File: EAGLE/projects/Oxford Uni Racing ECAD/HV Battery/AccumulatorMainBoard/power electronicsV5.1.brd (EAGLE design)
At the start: 167.6 x 103.8 mm, 82 parts, among them IC1 4043D, IC2 SE555D, IC9 4011D, K2 T9AS5D12-12=T9A, K6 T9AS1D12-48=T9A, K7 T9AS1D12-48=T9A, Q1 BSS138, Q2 BSS138, Q3 BSS138, Q4 BSS138

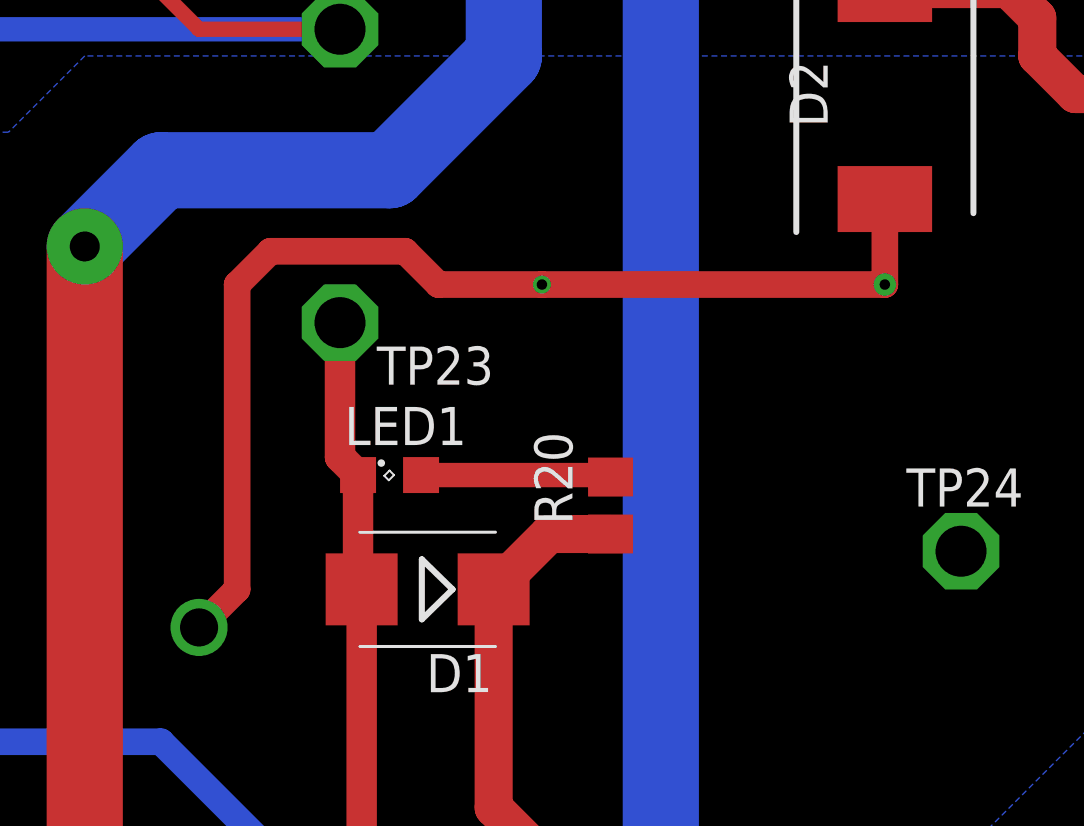
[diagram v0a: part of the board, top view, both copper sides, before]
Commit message: Mainboard v5.1
Fixes the +12V  connections
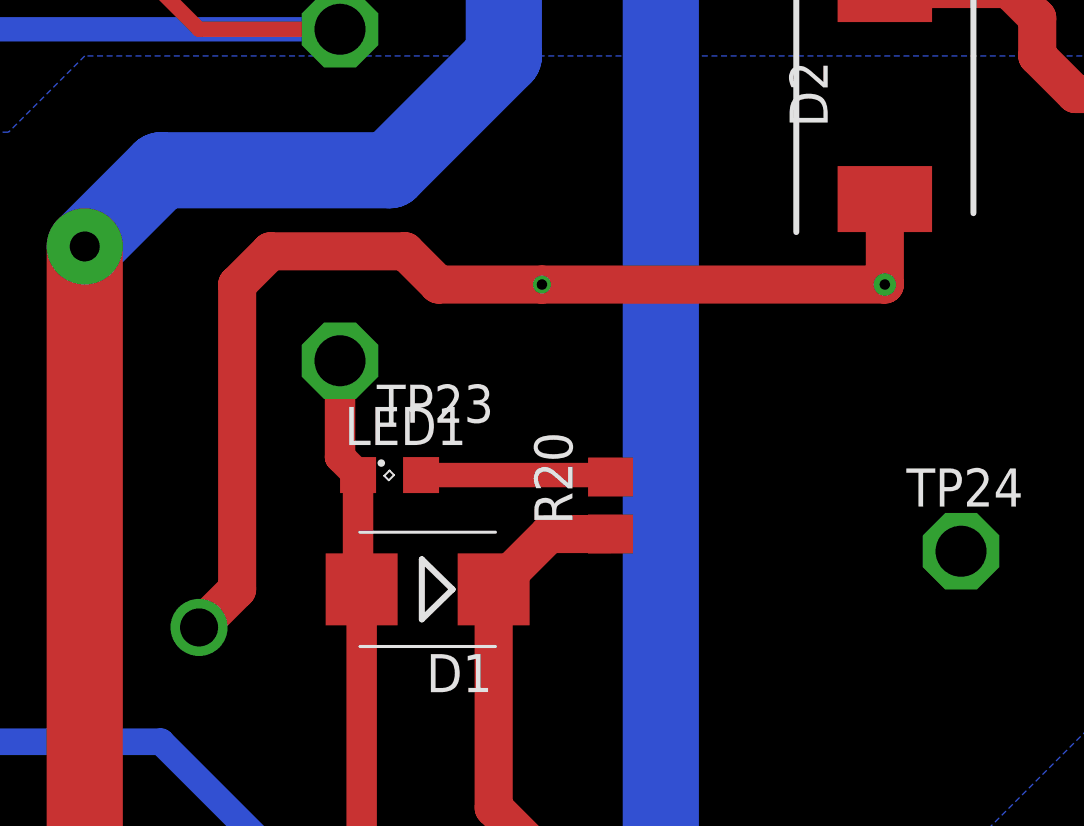
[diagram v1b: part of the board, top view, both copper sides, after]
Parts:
- moved TP23 1.27 mm to (93.6, 54.6)
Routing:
- net PRECHARGE_SELECT: track 133.7 -> 132.4 mm
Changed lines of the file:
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@@
 <attribute name="VALUE" x="40.132" y="52.832" size="0.0254" layer="27"/>
 </element>
-<element name="TP23" library="testpad" library_urn="urn:adsk.eagle:library:385" package="P1-17" package3d_urn="urn:adsk.eagle:package:27949/1" value="TPPAD1-17" x="93.599" y="55.88" smashed="yes">
-<attribute name="NAME" x="94.8271" y="53.8129" size="1.27" layer="25"/>
-<attribute name="POPULARITY" value="0" x="93.599" y="55.88" size="1.778" layer="27" display="off"/>
-<attribute name="TP_SIGNAL_NAME" value="" x="93.599" y="53.975" size="1" layer="37"/>
-<attribute name="VALUE" x="89.281" y="55.372" size="0.0254" layer="27"/>
+<element name="TP23" library="testpad" library_urn="urn:adsk.eagle:library:385" package="P1-17" package3d_urn="urn:adsk.eagle:package:27949/1" value="TPPAD1-17" x="93.599" y="54.61" smashed="yes">
+<attribute name="NAME" x="94.8271" y="52.5429" size="1.27" layer="25"/>
+<attribute name="POPULARITY" value="0" x="93.599" y="54.61" size="1.778" layer="27" display="off"/>
+<attribute name="TP_SIGNAL_NAME" value="" x="93.599" y="52.705" size="1" layer="37"/>
+<attribute name="VALUE" x="89.281" y="54.102" size="0.0254" layer="27"/>
 </element>
 <element name="TP4" library="testpad" library_urn="urn:adsk.eagle:library:385" package="P1-17" package3d_urn="urn:adsk.eagle:package:27949/1" value="TPPAD1-17" x="93.599" y="65.659" smashed="yes">
@@
 <wire x1="76.515" y1="68.834" x2="76.581" y2="68.834" width="1.016" layer="1"/>
 <via x="76.581" y="68.834" extent="1-16" drill="0.65" diameter="1.3"/>
-<wire x1="111.76" y1="60" x2="111.76" y2="57.15" width="0.889" layer="1"/>
+<wire x1="111.76" y1="60" x2="111.76" y2="57.15" width="1.27" layer="1"/>
 <via x="111.76" y="57.15" extent="1-16" drill="0.35" diameter="0.75"/>
 <wire x1="124.841" y1="60" x2="123.19" y2="58.349" width="0.889" layer="1"/>
@@
 <wire x1="80.01" y1="67.31" x2="80.01" y2="62.23" width="0.889" layer="1"/>
 <via x="80.01" y="62.23" extent="1-16" drill="0.6"/>
-<wire x1="88.9" y1="45.72" x2="90.17" y2="46.99" width="0.889" layer="1"/>
-<wire x1="90.17" y1="46.99" x2="90.17" y2="57.15" width="0.889" layer="1"/>
-<wire x1="90.17" y1="57.15" x2="91.27885" y2="58.25885" width="0.889" layer="1"/>
-<wire x1="91.27885" y1="58.25885" x2="95.7709375" y2="58.25885" width="0.889" layer="1"/>
-<wire x1="95.7709375" y1="58.25885" x2="96.8797875" y2="57.15" width="0.889" layer="1"/>
-<wire x1="96.8797875" y1="57.15" x2="100.33" y2="57.15" width="0.889" layer="1"/>
-<wire x1="100.33" y1="57.15" x2="111.76" y2="57.15" width="0.889" layer="1"/>
+<wire x1="88.9" y1="45.72" x2="90.17" y2="46.99" width="1.27" layer="1"/>
+<wire x1="90.17" y1="46.99" x2="90.17" y2="57.15" width="1.27" layer="1"/>
+<wire x1="90.17" y1="57.15" x2="91.27885" y2="58.25885" width="1.27" layer="1"/>
+<wire x1="91.27885" y1="58.25885" x2="95.7709375" y2="58.25885" width="1.27" layer="1"/>
+<wire x1="95.7709375" y1="58.25885" x2="96.8797875" y2="57.15" width="1.27" layer="1"/>
+<wire x1="96.8797875" y1="57.15" x2="100.33" y2="57.15" width="1.27" layer="1"/>
+<wire x1="100.33" y1="57.15" x2="111.76" y2="57.15" width="1.27" layer="1"/>
 </signal>
 <signal name="N$3" class="2">
@@
 <wire x1="94.2" y1="47.11" x2="94.2" y2="50.8" width="1.016" layer="1"/>
 <wire x1="94.2" y1="50.8" x2="93.599" y2="51.401" width="1.016" layer="1"/>
-<wire x1="93.599" y1="51.401" x2="93.599" y2="55.88" width="1.016" layer="1"/>
+<wire x1="93.599" y1="51.401" x2="93.599" y2="54.61" width="1.016" layer="1"/>
 <wire x1="8.89" y1="71.3486" x2="38.3286" y2="41.91" width="0.889" layer="16"/>
 <wire x1="38.3286" y1="41.91" x2="87.63" y2="41.91" width="0.889" layer="16"/>

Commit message: Final mainboard design
final mainboard design. v5.1
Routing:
- net +12V: track 147.5 -> 132.4 mm
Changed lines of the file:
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@@
 <attribute name="POPULARITY" value="0" x="59.309" y="47.879" size="1.778" layer="27" display="off"/>
 <attribute name="TP_SIGNAL_NAME" value="" x="59.309" y="47.879" size="1.778" layer="27" display="off"/>
-<attribute name="VALUE" x="59.309" y="46.609" size="0.0254" layer="27"/>
+<attribute name="VALUE" x="59.309" y="46.609" size="0.0254" layer="1"/>
 </element>
 <element name="TP11" library="testpad" library_urn="urn:adsk.eagle:library:385" package="P1-17" package3d_urn="urn:adsk.eagle:package:27949/1" value="TPPAD1-17" x="54.483" y="84.836" smashed="yes">
@@
 <wire x1="98.72" y1="46.99" x2="100.564" y2="48.834" width="1.27" layer="1"/>
 <wire x1="100.564" y1="48.834" x2="102.616" y2="48.834" width="1.27" layer="1"/>
-<wire x1="66.04" y1="31.75" x2="66.04" y2="44.282" width="1.27" layer="1"/>
-<wire x1="66.04" y1="44.282" x2="76.454" y2="54.696" width="1.27" layer="1"/>
 <wire x1="30.48" y1="31.75" x2="30.48" y2="45.38" width="1.27" layer="1"/>
 <wire x1="30.48" y1="45.38" x2="30.82" y2="45.72" width="1.27" layer="1"/>
@@
 <vertex x="133.35" y="60.96"/>
 <vertex x="129.54" y="64.77"/>
-<vertex x="85.09" y="64.77"/>
-<vertex x="82.55" y="62.23"/>
-<vertex x="81.28" y="62.23"/>
+<vertex x="78.74" y="64.77"/>
 <vertex x="77.47" y="66.04"/>
-<vertex x="77.47" y="71.12"/>
-<vertex x="76.2" y="72.39"/>
+<vertex x="77.47" y="72.39"/>
 <vertex x="72.39" y="72.39"/>
 <vertex x="69.85" y="69.85"/>
@@
 <wire x1="107.95" y1="30.48" x2="98.72" y2="39.71" width="1.27" layer="1"/>
 <via x="100.33" y="57.15" extent="1-16" drill="0.35"/>
-<wire x1="72.39" y1="45.72" x2="68.58" y2="41.91" width="2.54" layer="1"/>
-<wire x1="68.58" y1="34.29" x2="66.04" y2="31.75" width="2.54" layer="1"/>
-<wire x1="68.58" y1="41.91" x2="68.58" y2="34.29" width="2.54" layer="1"/>
-<via x="72.39" y="45.72" extent="1-16" drill="1.27"/>
+<wire x1="72.39" y1="38.1" x2="66.04" y2="31.75" width="2.54" layer="1"/>
+<wire x1="72.39" y1="45.72" x2="72.39" y2="38.1" width="2.54" layer="1"/>
 <via x="88.9" y="45.72" extent="1-16" drill="1.27"/>
 <wire x1="76.581" y1="68.834" x2="78.486" y2="68.834" width="0.889" layer="1"/>
@@
 <wire x1="96.8797875" y1="57.15" x2="100.33" y2="57.15" width="1.27" layer="1"/>
 <wire x1="100.33" y1="57.15" x2="111.76" y2="57.15" width="1.27" layer="1"/>
+<wire x1="72.39" y1="45.72" x2="72.39" y2="53.172" width="0.889" layer="1"/>
+<wire x1="76.454" y1="54.696" x2="73.914" y2="54.696" width="0.889" layer="1"/>
+<wire x1="73.914" y1="54.696" x2="72.39" y2="53.172" width="0.889" layer="1"/>
+<via x="72.39" y="45.72" extent="1-16" drill="1.27" diameter="2.54"/>
 </signal>
 <signal name="N$3" class="2">

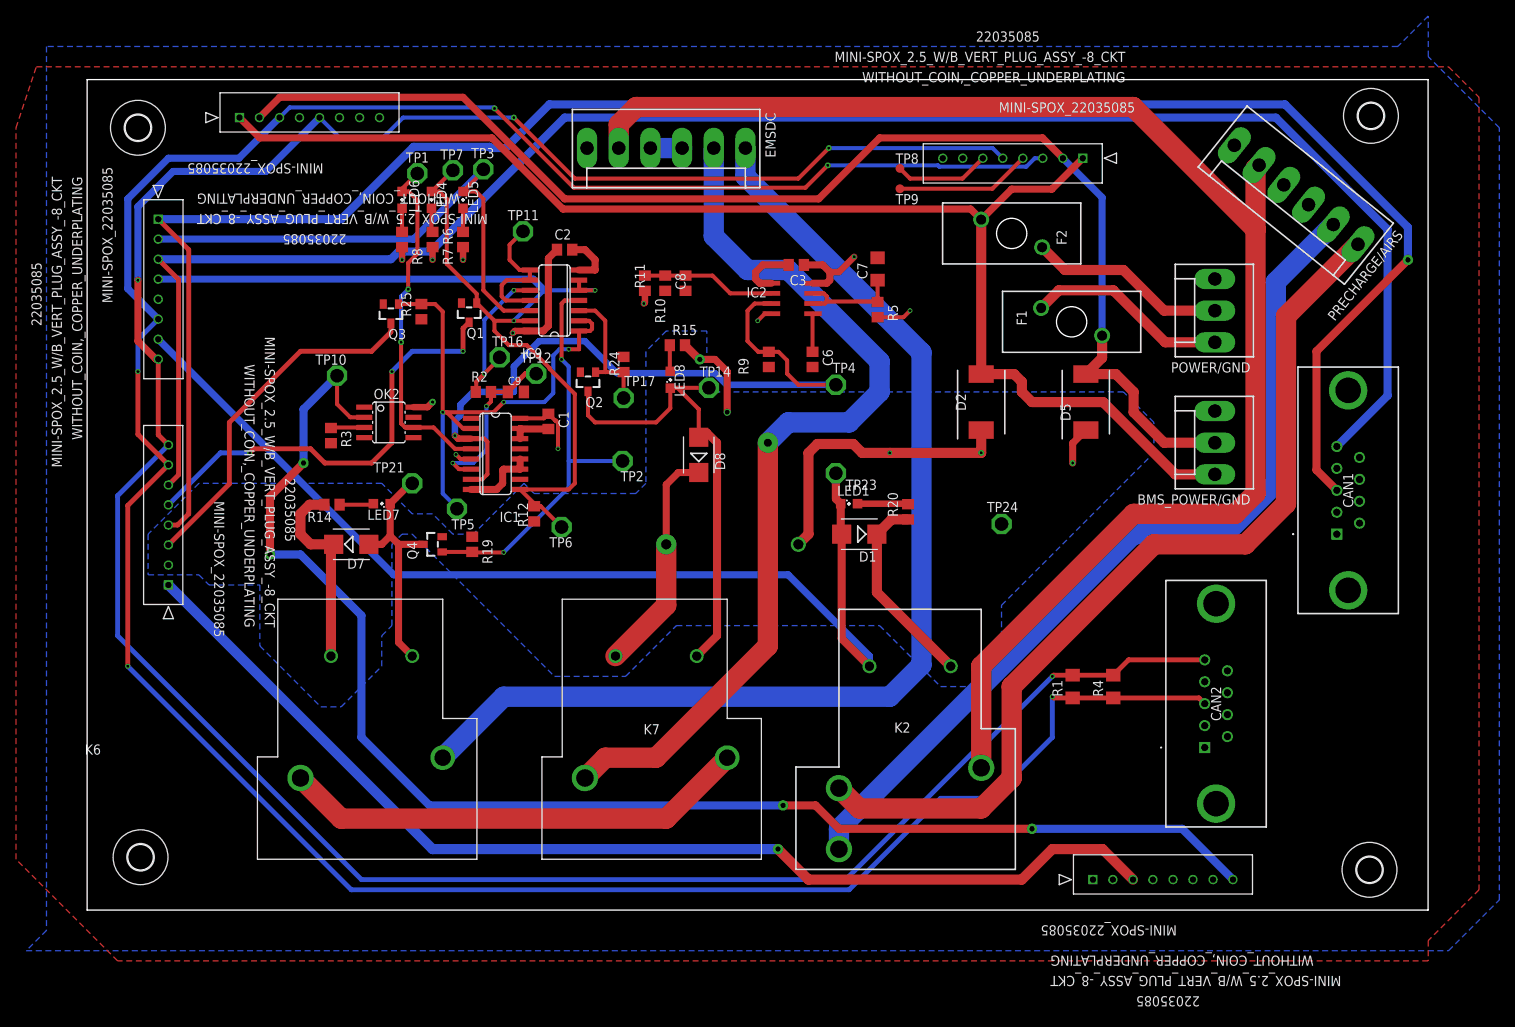
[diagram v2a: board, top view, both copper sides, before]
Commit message: Final final mainboard Design (v5.1)
Adds termination resistors to Can 1. Updates silkscreen. Connects Power plane islands. 
Passes design rule check, verified the CAM files using PCBway gerber viewer

To do list (if have time): 
change to resettable fuses; add OUR logo (haven't figured out how)
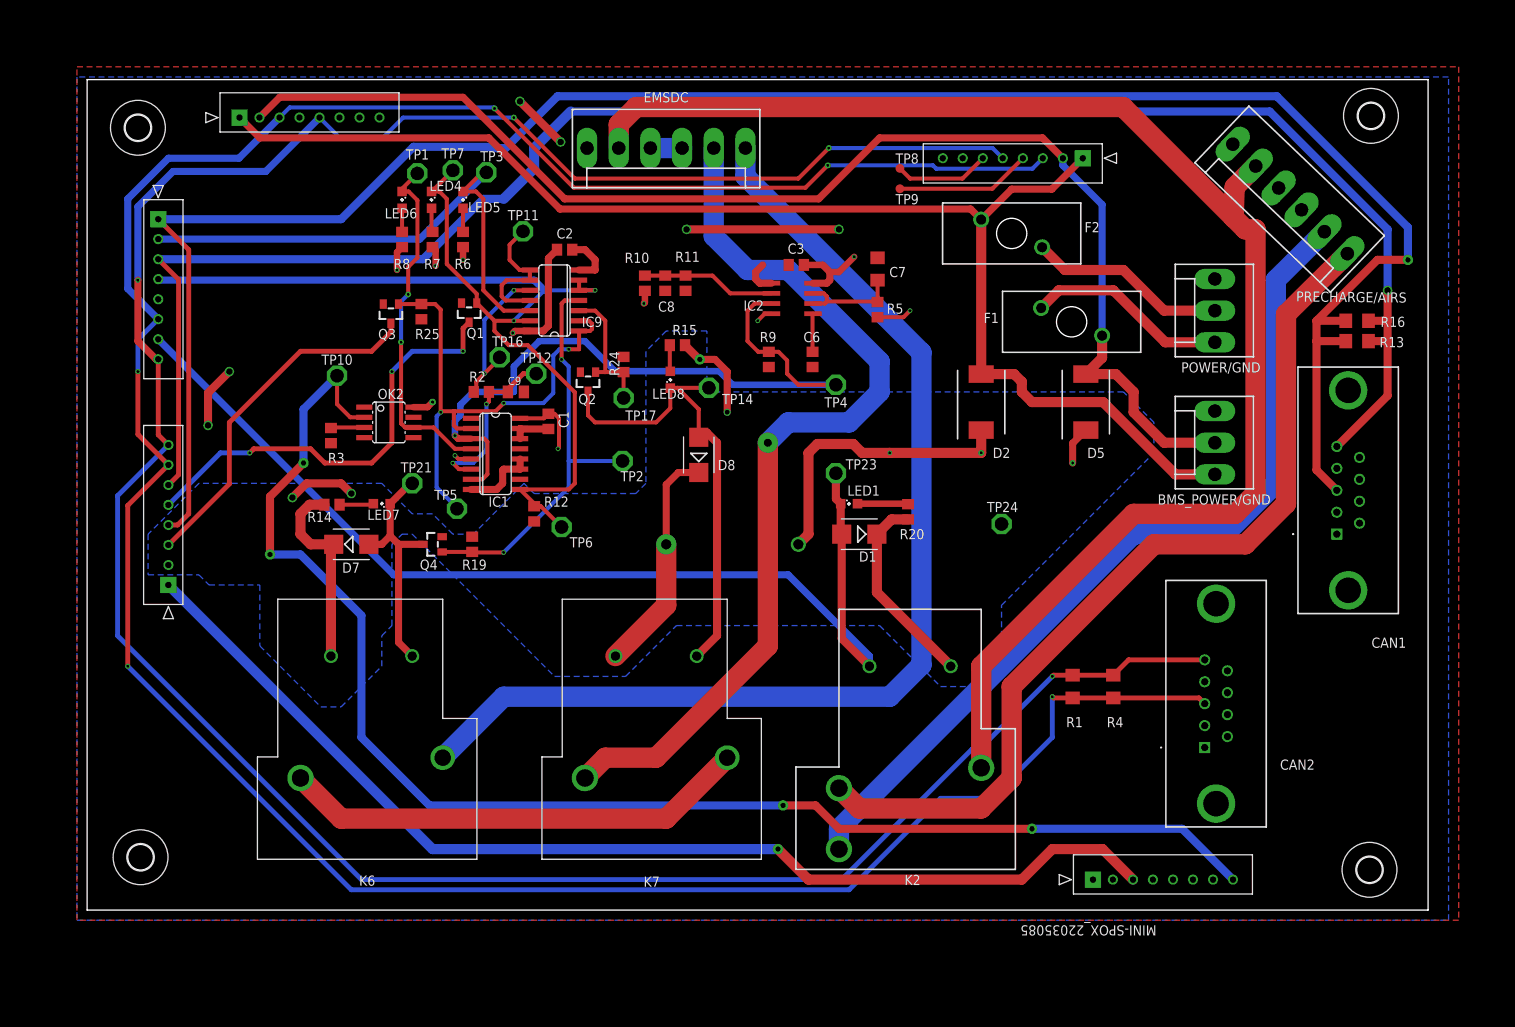
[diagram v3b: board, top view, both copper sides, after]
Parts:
- added R13, R16: 120, rcl:R1206
- moved PRECHARGE/AIRS 0.92 mm to (150.4, 88.9), turned to 136.3 degrees
- moved TP3 0.54 mm to (49.9, 92.2)
- moved R2 0.25 mm to (49.3, 64.8)
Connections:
- net CAN1_H: now also R13.1, R16.1
- net CAN1_L: now also R13.2, R16.2
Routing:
- net +3V3: track 52.6 -> 89.7 mm, vias 11 -> 17
- net CAN1_H: track 248.8 -> 259.2 mm
- net +12V: track 132.4 -> 141.0 mm, vias 7 -> 9
- net CAN1_L: track 226.4 -> 233.3 mm, vias 0 -> 1
- net GND: track 28.5 -> 25.3 mm
- net N$3: track 115.6 -> 113.9 mm
- net N$12: track 110.4 -> 109.0 mm
- net N$11: track 187.0 -> 186.3 mm

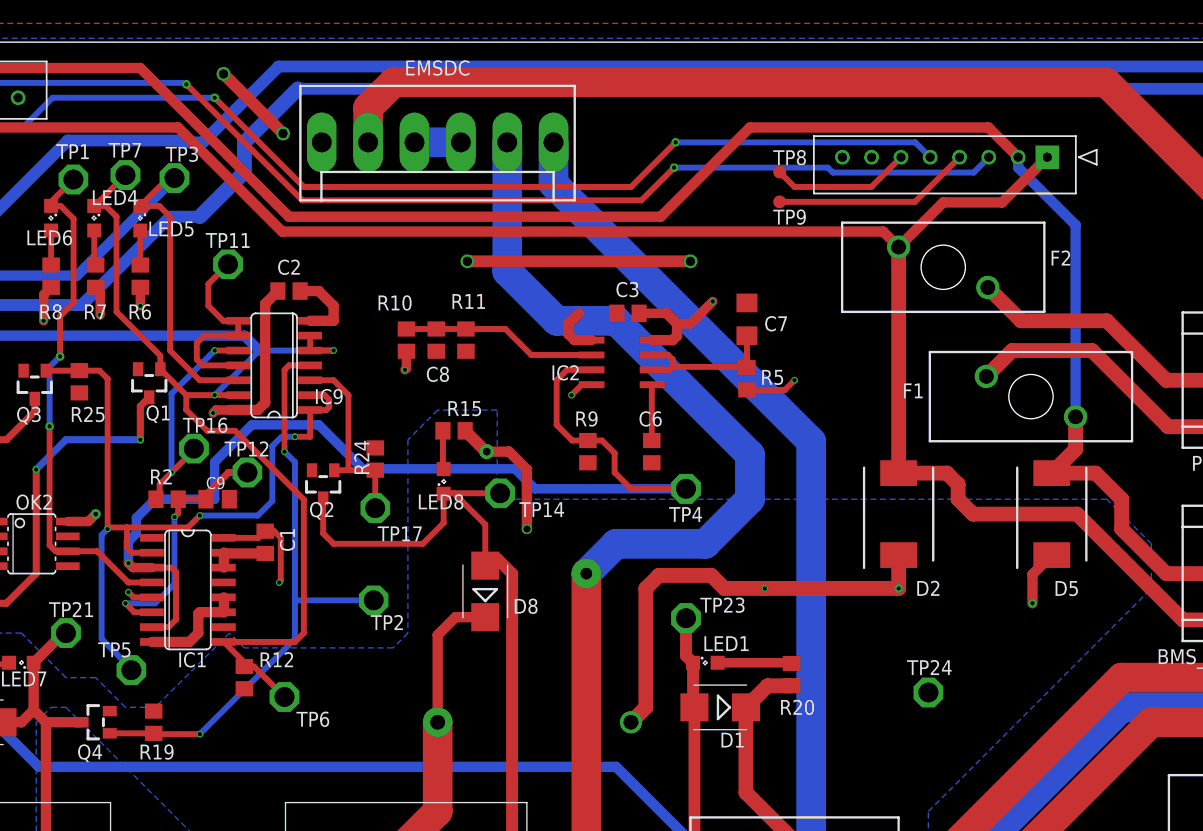
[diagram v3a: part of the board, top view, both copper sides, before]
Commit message: FINAL FINLAL FINAL mainboard design
Changes the fuses from car fuses to 2.5A resettable fuses. Adds the OUR logo and designers. Moves LED to more logical locations
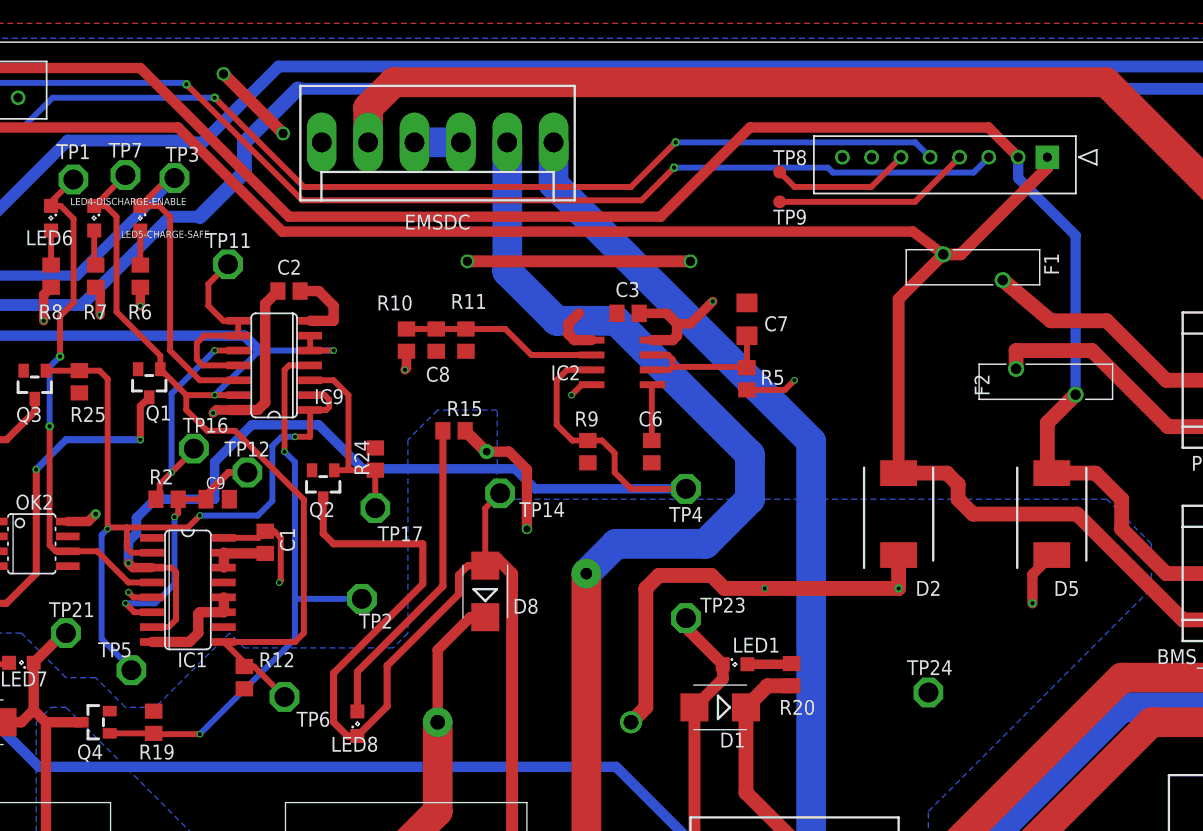
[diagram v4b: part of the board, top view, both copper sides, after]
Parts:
- F1, F2: value 01530008Z -> DIP-PPTC-2.5A-30V(D11.4MM); device SamacSys_Parts:01530008 -> DIP-PPTC-2.5A-30V_D11.4MM_:F2-5.1-11.4X3.0X18.3MM
- moved LED8 22.0 mm to (65.5, 45.6)
- moved LED1 2.54 mm to (97.8, 50.7)
- moved F2 2.54 mm to (118.1, 84.6), turned to 0 degrees
- moved F1 1.80 mm to (124.3, 74.8), turned to 180 degrees
- moved TP2 1.02 mm to (65.9, 56.3)
- renumbered LED4 to LED4-DISCHARGE-ENABLE, LED5 to LED5-CHARGE-SAFE
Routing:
- net IMD_COIL_OUT: track 59.8 -> 90.2 mm
- net N$20: track 3.29 -> 27.0 mm
- net N$22: track 6.34 -> 3.80 mm
- net PRECHARGE_SELECT: track 132.4 -> 134.4 mm
- net N$4: track 25.3 -> 23.4 mm
- net READY_POWER: track 168.3 -> 170.2 mm
- net N$2: track 24.9 -> 23.7 mm
- net N$16: track 51.6 -> 50.6 mm
- net +12V: track 141.0 -> 140.3 mm
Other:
- board text added: "/Users/liuxianming/Downloads/OUR new logo navy.bmp"
- board text added: "Designed by: Xianming Liu, James Willy, Aminah Dixon, Omar Ahmed"
